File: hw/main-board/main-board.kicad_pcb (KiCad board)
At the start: 2 copper layers, 42 x 42 mm, 68 parts, among them J1 USB_C_Receptacle_USB2.0_16P, J2 S4B-XH-A_LF__SN_, J3 S4B-XH-A_LF__SN_, J4 Conn_ARM_JTAG_SWD_10, Q1 AONR21307, U1 HUSB238_xxxDD, U2 AP63205WU, U3 AP2112K-3.3, U4 PTR54L, U5 TMC2226-SA, U6 TMC2226-SA, U7 KTD2026BEWE-TR

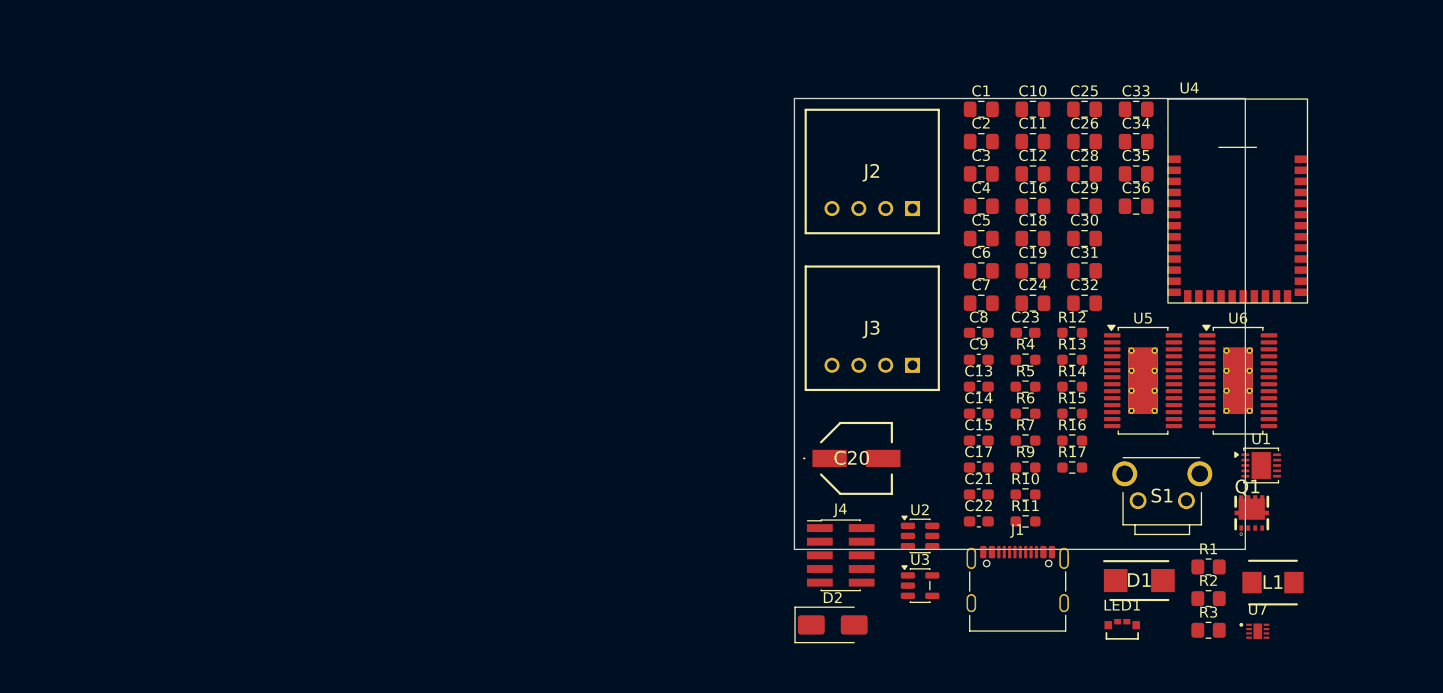
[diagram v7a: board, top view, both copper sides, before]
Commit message: Change board outline to 50x50, add replicate layout for second TMC2226
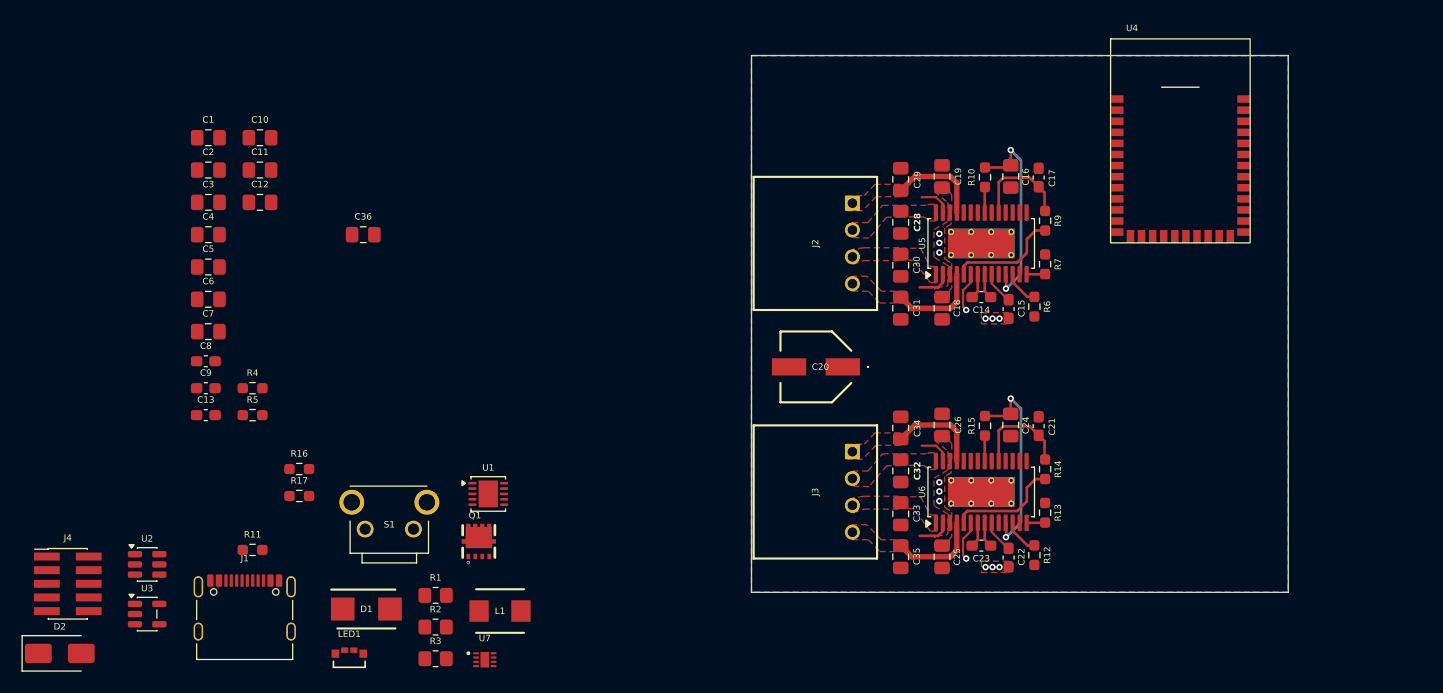
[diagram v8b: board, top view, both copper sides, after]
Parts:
- moved C13 72.0 mm to (69.7, 103.0)
- moved C36 72.0 mm to (84.3, 86.2)
- moved C8 72.0 mm to (69.7, 98.0)
- moved C9 72.0 mm to (69.7, 100.5)
- moved LED1 72.0 mm to (82.6, 124.9)
- moved Q1 72.0 mm to (95.1, 114.8)
- moved U2 72.0 mm to (64.2, 116.9)
- moved U3 72.0 mm to (64.2, 121.5)
- moved C1 72.0 mm to (69.9, 77.2)
- moved C10 72.0 mm to (74.7, 77.2)
- moved C11 72.0 mm to (74.7, 80.2)
- moved C12 72.0 mm to (74.7, 83.2)
- moved C2 72.0 mm to (69.9, 80.2)
- moved C3 72.0 mm to (69.9, 83.2)
- moved C4 72.0 mm to (69.9, 86.2)
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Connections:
- J2 pad 1: Net-(U5-OB2) -> Net-(U5-OA2)
- J2 pad 2: Net-(U5-OB1) -> Net-(U5-OA1)
- J2 pad 3: Net-(U5-OA2) -> Net-(U5-OB1)
- J2 pad 4: Net-(U5-OA1) -> Net-(U5-OB2)
- J3 pad 1: Net-(U6-OB2) -> Net-(U6-OA2)
- J3 pad 2: Net-(U6-OB1) -> Net-(U6-OA1)
- J3 pad 3: Net-(U6-OA2) -> Net-(U6-OB1)
- J3 pad 4: Net-(U6-OA1) -> Net-(U6-OB2)
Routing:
- net GND: track 0.00 -> 19.8 mm, vias 0 -> 2
- net /VREF1: track 0.00 -> 19.2 mm, vias 0 -> 2
- net /VREF2: track 0.00 -> 19.2 mm, vias 0 -> 2
- net +3.3V: track 0.00 -> 19.1 mm
- net /EN2: track 0.00 -> 10.5 mm
- net /EN1: track 0.00 -> 10.5 mm
- net Net-(U6-OA2): track 0.00 -> 8.91 mm
- net Net-(U5-OA2): track 0.00 -> 8.91 mm
- net Net-(U6-OB2): track 0.00 -> 8.61 mm
- net Net-(U5-OB2): track 0.00 -> 8.61 mm
- net Net-(U5-MS1_AD0): track 0.00 -> 3.32 mm
- net Net-(U6-MS1_AD0): track 0.00 -> 3.32 mm
- net Net-(U5-VCP): track 0.00 -> 3.06 mm
- net Net-(U6-VCP): track 0.00 -> 3.06 mm
- net Net-(U6-VREF): track 0.00 -> 2.51 mm
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- added copper zone on B.Cu, net GND
- added copper zone on F.Cu, net GND
- added copper zone on In1.Cu, net GND
- added copper zone on F.Cu, net Net-(U5-OA1)
- added copper zone on F.Cu, net Net-(U5-OA2)
- added copper zone on F.Cu, net Net-(U5-OB1)
- added copper zone on F.Cu, net Net-(U5-OB2)
- added copper zone on F.Cu, net Net-(U6-OA1)
- added copper zone on F.Cu, net Net-(U6-OA2)
- added copper zone on F.Cu, net Net-(U6-OB1)
- added copper zone on F.Cu, net Net-(U6-OB2)
- added copper zone on F.Cu, net VBUS
- added copper zone on In1.Cu, net VBUS
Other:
- board size 42 x 42 mm -> 50 x 50 mm
- copper layers 2 -> 4
